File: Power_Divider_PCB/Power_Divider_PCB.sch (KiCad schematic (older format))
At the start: 9 parts, among them J1 Conn_02x02_Counter_Clockwise, J2 Conn_01x02, J3 Conn_02x02_Counter_Clockwise, J4 Conn_02x02_Counter_Clockwise, J5 Conn_02x02_Counter_Clockwise, J6 Conn_02x02_Counter_Clockwise, J7 Conn_02x02_Counter_Clockwise, J8 Conn_01x02, J9 Conn_01x02

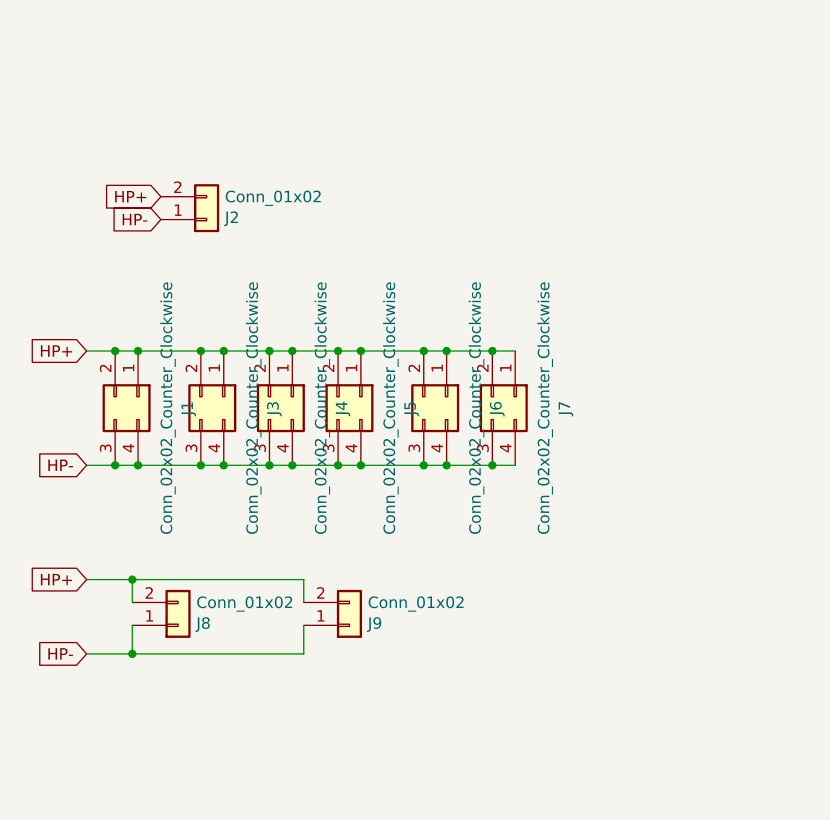
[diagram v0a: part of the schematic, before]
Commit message: Added one extra XT connector, moved existing molexes. Added Voltage polarization check: green LED - OK, red LED - wrong.
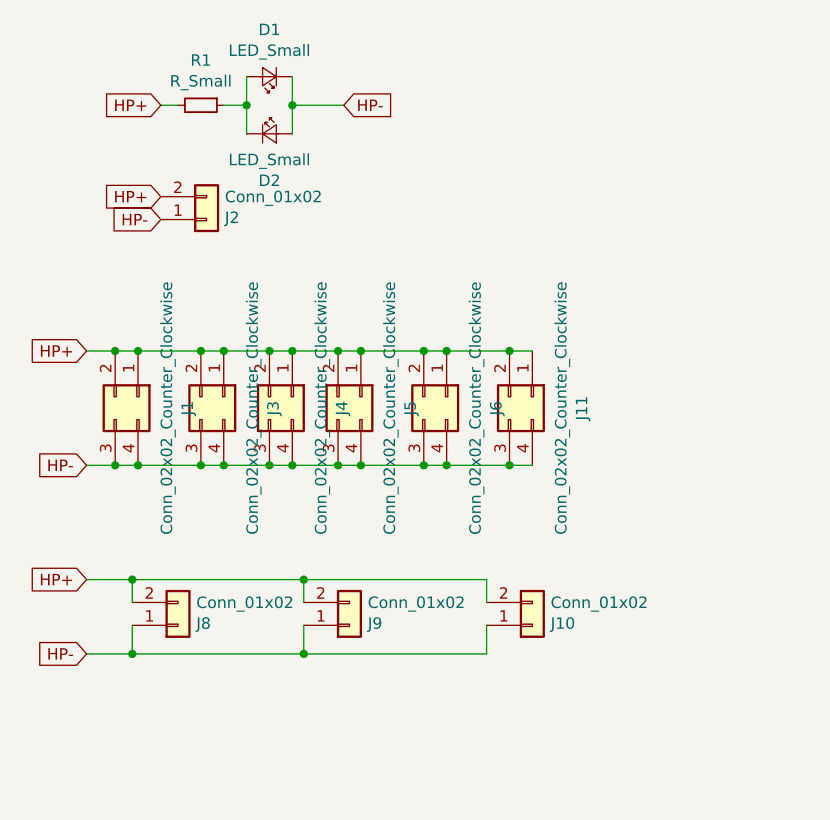
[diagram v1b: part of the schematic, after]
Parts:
- removed J7: Conn_02x02_Counter_Clockwise, Connector_Molex:Molex_Mini-Fit_Jr_5566-04A_2x02_P4.20mm_Vertical, symbol Connector_Generic:Conn_02x02_Counter_Clockwise
- added D1, D2: LED_Small, LED_THT:LED_D3.0mm, symbol Device:LED_Small
- added J10: Conn_01x02, Connectors:XT90PW-F, symbol Connector_Generic:Conn_01x02
- added J11: Conn_02x02_Counter_Clockwise, Connector_Molex:Molex_Mini-Fit_Jr_5566-04A_2x02_P4.20mm_Vertical, symbol Connector_Generic:Conn_02x02_Counter_Clockwise
- added R1: R_Small, Resistor_THT:R_Axial_DIN0207_L6.3mm_D2.5mm_P7.62mm_Horizontal, symbol Device:R_Small
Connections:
- net HP+: now also J10.2 (Pin_2), J11.1 (Pin_1), J11.2 (Pin_2), R1.2
- net HP-: now also D1.1 (K), D2.2 (A), J10.1 (Pin_1), J11.3 (Pin_3), J11.4 (Pin_4)
- new net: D1.2 (A), D2.1 (K), R1.1
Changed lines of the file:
@@
 Text GLabel 4550 3525 0    50   Input ~ 0
 HP-
-Wire Wire Line
-	6325 3025 6425 3025
-Wire Wire Line
-	6125 3025 6325 3025
-Connection ~ 6325 3025
-Wire Wire Line
-	6125 3525 6325 3525
-Connection ~ 6325 3525
-Wire Wire Line
-	6325 3525 6425 3525
 Connection ~ 6125 3525
 Connection ~ 6025 3525
@@
 Wire Wire Line
 	4550 3025 4675 3025
-$Comp
-L Connector_Generic:Conn_02x02_Counter_Clockwise J7
-U 1 1 5E504832
-P 6425 3225
-F 0 "J7" H 6475 3442 50  0000 C CNN
-F 1 "Conn_02x02_Counter_Clockwise" H 6475 3351 50  0000 C CNN
-F 2 "Connector_Molex:Molex_Mini-Fit_Jr_5566-04A_2x02_P4.20mm_Vertical" H 6425 3225 50  0001 C CNN
-F 3 "~" H 6425 3225 50  0001 C CNN
-	1    6425 3225
-	0    1    1    0
-$EndComp
 $Comp
 L Connector_Generic:Conn_02x02_Counter_Clockwise J6
@@
 Text Notes 7080 6900 0    118  ~ 0
 Igor Zieliński
+$Comp
+L Connector_Generic:Conn_01x02 J10
+U 1 1 5E501641
+P 6500 4225
+F 0 "J10" H 6580 4217 50  0000 L CNN
+F 1 "Conn_01x02" H 6580 4126 50  0000 L CNN
+F 2 "Connectors:XT90PW-F" H 6500 4225 50  0001 C CNN
+F 3 "~" H 6500 4225 50  0001 C CNN
+	1    6500 4225
+	1    0    0    1
+$EndComp
+Wire Wire Line
+	5500 4025 6300 4025
+Wire Wire Line
+	6300 4025 6300 4125
+Connection ~ 5500 4025
+Wire Wire Line
+	5500 4350 6300 4350
+Wire Wire Line
+	6300 4350 6300 4225
+Connection ~ 5500 4350
+$Comp
+L Connector_Generic:Conn_02x02_Counter_Clockwise J11
+U 1 1 5E50702B
+P 6500 3225
+F 0 "J11" H 6550 3442 50  0000 C CNN
+F 1 "Conn_02x02_Counter_Clockwise" H 6550 3351 50  0000 C CNN
+F 2 "Connector_Molex:Molex_Mini-Fit_Jr_5566-04A_2x02_P4.20mm_Vertical" H 6500 3225 50  0001 C CNN
+F 3 "~" H 6500 3225 50  0001 C CNN
+	1    6500 3225
+	0    1    1    0
+$EndComp
+Wire Wire Line
+	6125 3025 6400 3025
+Wire Wire Line
+	6125 3525 6400 3525
+Wire Wire Line
+	6400 3525 6500 3525
+Connection ~ 6400 3525
+Wire Wire Line
+	6400 3025 6500 3025
+Connection ~ 6400 3025
+$Comp
+L Device:LED_Small D1
+U 1 1 5E5168AB
+P 5350 1825
+F 0 "D1" H 5350 1620 50  0000 C CNN
+F 1 "LED_Small" H 5350 1711 50  0000 C CNN
+F 2 "LED_THT:LED_D3.0mm" V 5350 1825 50  0001 C CNN
+F 3 "~" V 5350 1825 50  0001 C CNN
+	1    5350 1825
+	-1   0    0    1
+$EndComp
+$Comp
+L Device:LED_Small D2
+U 1 1 5E518E7C
+P 5350 2075
+F 0 "D2" H 5350 1870 50  0000 C CNN
+F 1 "LED_Small" H 5350 1961 50  0000 C CNN
+F 2 "LED_THT:LED_D3.0mm" V 5350 2075 50  0001 C CNN
+F 3 "~" V 5350 2075 50  0001 C CNN
+	1    5350 2075
+	1    0    0    -1
+$EndComp
+Text GLabel 4875 1950 0    50   Input ~ 0
+HP+
+Wire Wire Line
+	5450 1825 5450 1950
+Text GLabel 5675 1950 2    50   Input ~ 0
+HP-
+Wire Wire Line
+	5675 1950 5450 1950
+Connection ~ 5450 1950
+Wire Wire Line
+	5450 1950 5450 2075
+Wire Wire Line
+	5250 1825 5250 1950
+$Comp
+L Device:R_Small R1
+U 1 1 5E51E727
+P 5050 1950
+F 0 "R1" V 4854 1950 50  0000 C CNN
+F 1 "R_Small" V 4945 1950 50  0000 C CNN
+F 2 "Resistor_THT:R_Axial_DIN0207_L6.3mm_D2.5mm_P7.62mm_Horizontal" H 5050 1950 50  0001 C CNN
+F 3 "~" H 5050 1950 50  0001 C CNN
+	1    5050 1950
+	0    1    1    0
+$EndComp
+Wire Wire Line
+	5150 1950 5250 1950
+Connection ~ 5250 1950
+Wire Wire Line
+	5250 1950 5250 2075
+Wire Wire Line
+	4875 1950 4950 1950
 $EndSCHEMATC
